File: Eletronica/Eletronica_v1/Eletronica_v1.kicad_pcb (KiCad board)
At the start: 2 copper layers, 3 parts, among them U1 QTR-1A_REFLECTANCE_SENSOR, U2 TB6612FNG

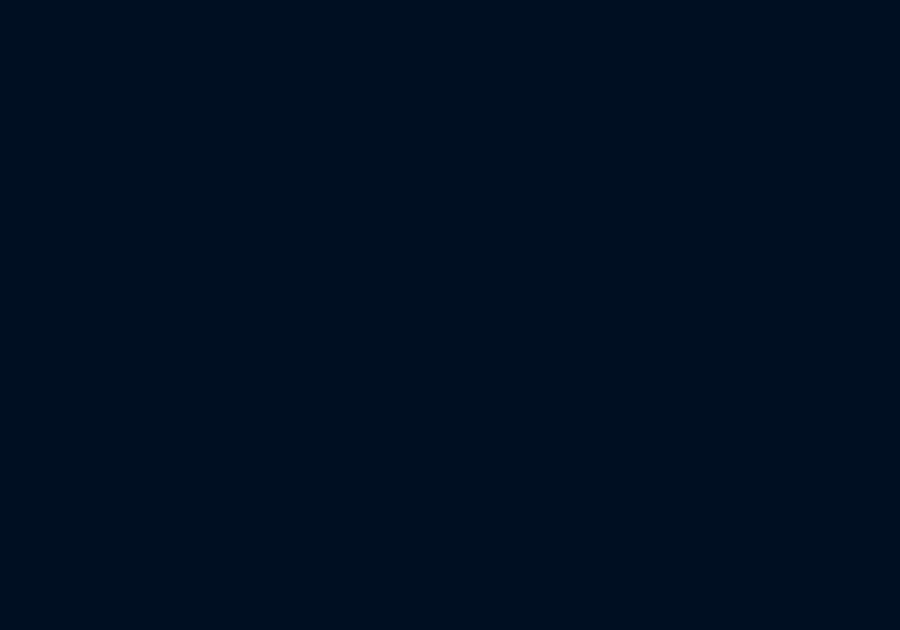
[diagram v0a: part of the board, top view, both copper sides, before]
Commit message: Corrigido circuito de alimentação e conexão dos periféricos
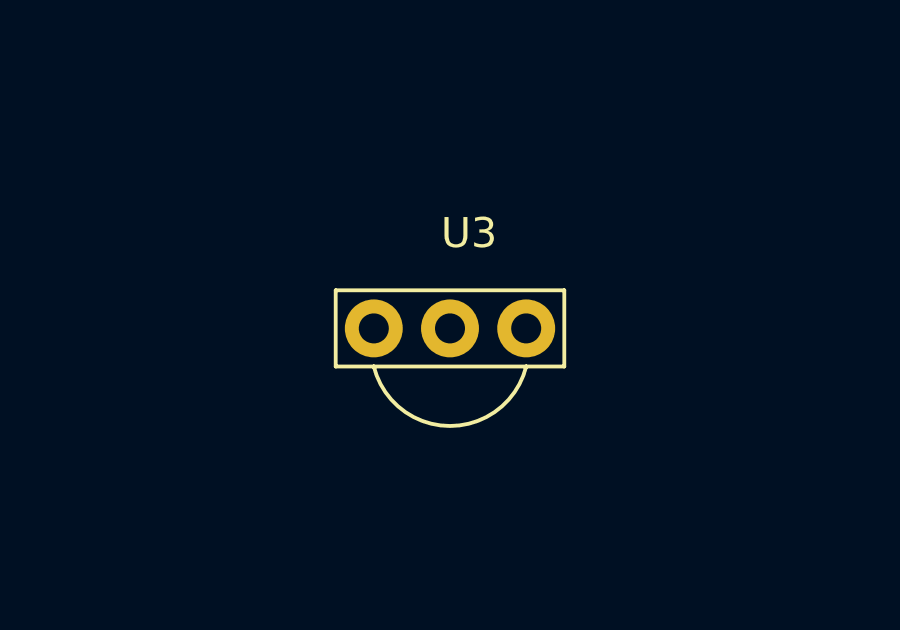
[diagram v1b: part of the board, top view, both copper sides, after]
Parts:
- added U3: TSOP1838, TSOP1838:TSOP1838, F.Cu at (118.4, 69.3)

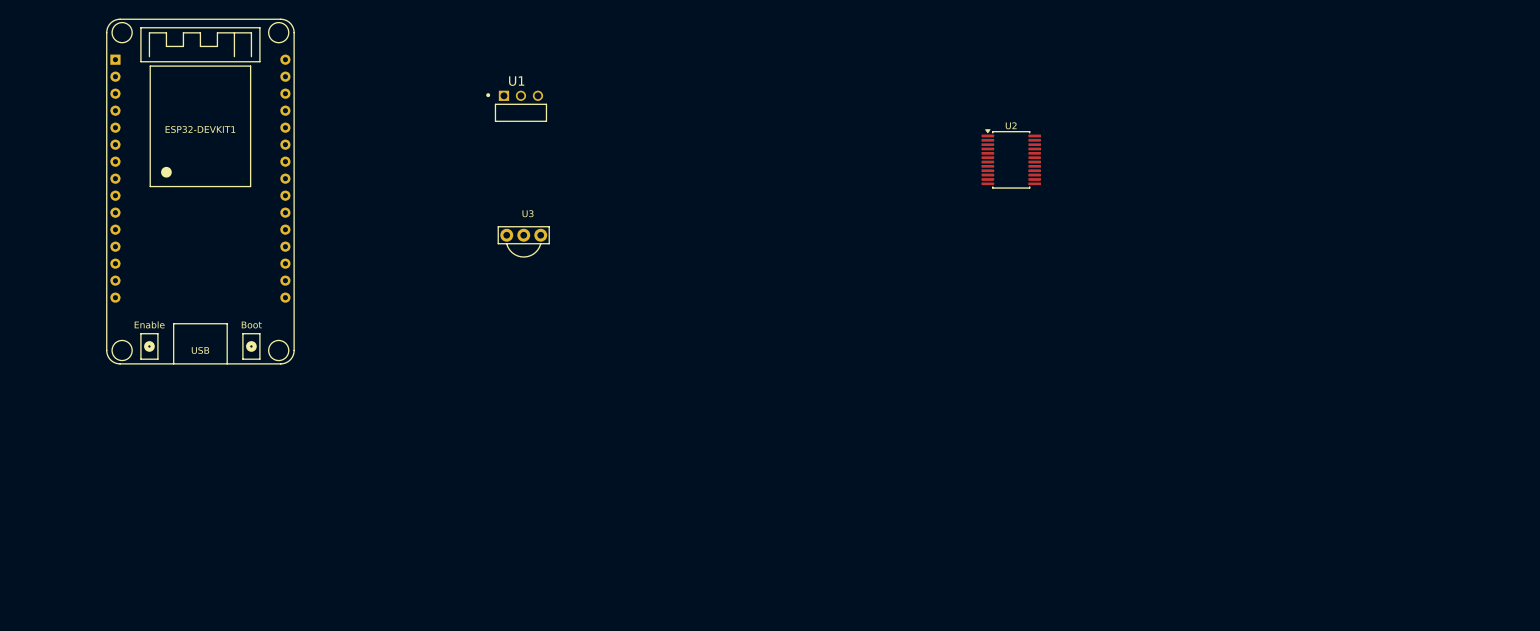
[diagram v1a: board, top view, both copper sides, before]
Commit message: Atualizado swtich e footprints
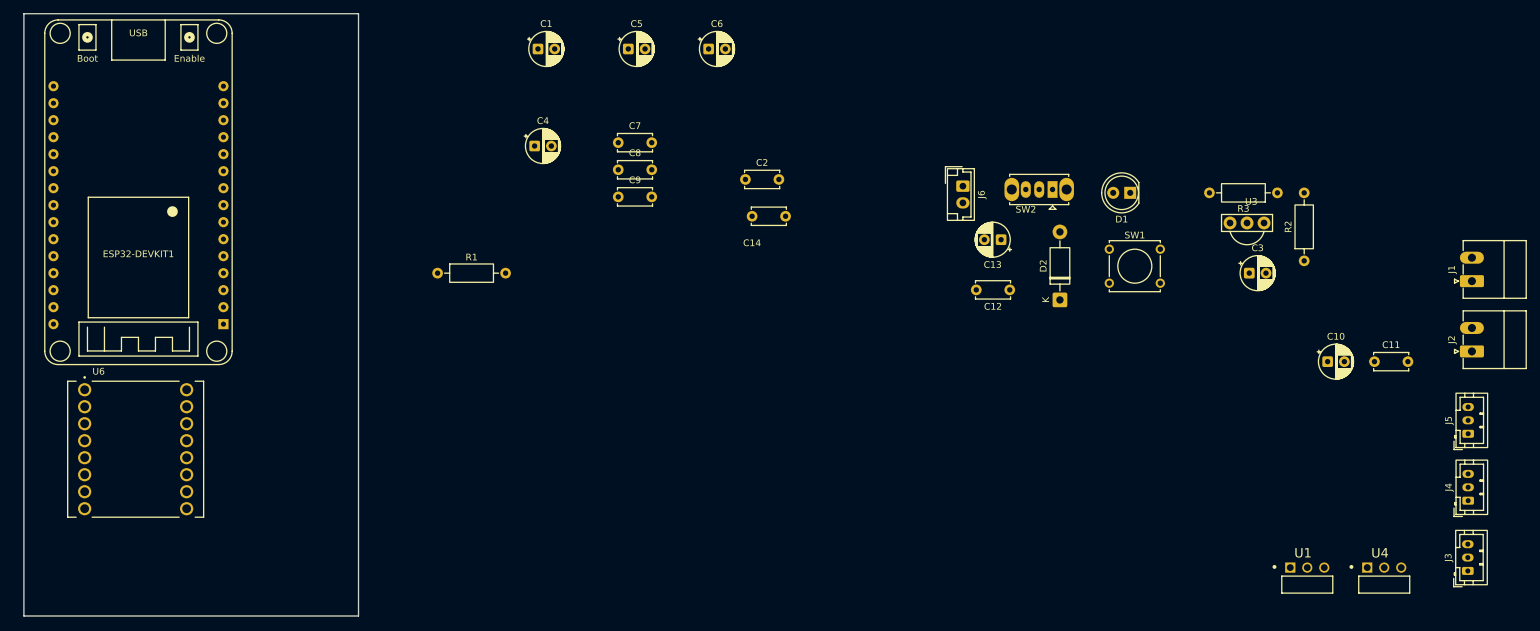
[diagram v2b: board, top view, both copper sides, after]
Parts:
- removed U2: TB6612FNG, Package_SO:SSOP-24_5.3x8.2mm_P0.65mm
- added C1: 10uF, Capacitor_THT:CP_Radial_D5.0mm_P2.50mm, F.Cu at (120.5, 41.5)
- added C10: 10uF, Capacitor_THT:CP_Radial_D5.0mm_P2.50mm, F.Cu at (238.5, 88.2)
- added C11: 100nF, Capacitor_THT:C_Disc_D5.0mm_W2.5mm_P5.00mm, F.Cu at (245.5, 88.2)
- added C12: 100nF, Capacitor_THT:C_Disc_D5.0mm_W2.5mm_P5.00mm, F.Cu at (191.0, 77.5)
- added C13: 10uF, Capacitor_THT:CP_Radial_D5.0mm_P2.50mm, F.Cu at (189.7, 70.0)
- added C14: 100nF, Capacitor_THT:C_Disc_D5.0mm_W2.5mm_P5.00mm, F.Cu at (152.5, 66.5)
- added C2: 100nF, Capacitor_THT:C_Disc_D5.0mm_W2.5mm_P5.00mm, F.Cu at (151.5, 61.0)
- added C3: 4.7uF, Capacitor_THT:CP_Radial_D5.0mm_P2.50mm, F.Cu at (226.8, 75.0)
- added C4: 10uF, Capacitor_THT:CP_Radial_D5.0mm_P2.50mm, F.Cu at (120.0, 56.0)
- added C5: 10uF, Capacitor_THT:CP_Radial_D5.0mm_P2.50mm, F.Cu at (134.0, 41.5)
- added C6: 10uF, Capacitor_THT:CP_Radial_D5.0mm_P2.50mm, F.Cu at (146.0, 41.5)
- added C7: 100nF, Capacitor_THT:C_Disc_D5.0mm_W2.5mm_P5.00mm, F.Cu at (132.5, 55.5)
- added C8: 100nF, Capacitor_THT:C_Disc_D5.0mm_W2.5mm_P5.00mm, F.Cu at (132.5, 59.5)
- added C9: 100nF, Capacitor_THT:C_Disc_D5.0mm_W2.5mm_P5.00mm, F.Cu at (132.5, 63.6)
- added D1: LED, LED_THT:LED_D5.0mm, F.Cu at (209.0, 63.0)
- added D2: 1N4007, Diode_THT:D_DO-41_SOD81_P10.16mm_Horizontal, F.Cu at (198.5, 79.0)
- added J1: Motor_R, Connector_Phoenix_MC:PhoenixContact_MC_1,5_2-G-3.5_1x02_P3.50mm_Horizontal, F.Cu at (260.1, 76.2)
- added J2: Motor_L, Connector_Phoenix_MC:PhoenixContact_MC_1,5_2-G-3.5_1x02_P3.50mm_Horizontal, F.Cu at (260.1, 86.7)
- added J3: Sharp_G2Y0A41SK, Connector_JST:JST_PH_B3B-PH-K_1x03_P2.00mm_Vertical, F.Cu at (259.4, 119.5)
- added J4: Sharp_G2Y0A41SK, Connector_JST:JST_PH_B3B-PH-K_1x03_P2.00mm_Vertical, F.Cu at (259.5, 109.0)
- added J5: Sharp_G2Y0A41SK, Connector_JST:JST_PH_B3B-PH-K_1x03_P2.00mm_Vertical, F.Cu at (259.5, 99.0)
- added J6: Bateria, Connector_JST:JST_EH_B2B-EH-A_1x02_P2.50mm_Vertical, F.Cu at (184.0, 62.0)
- added R1: 300, Resistor_THT:R_Axial_DIN0207_L6.3mm_D2.5mm_P10.16mm_Horizontal, F.Cu at (105.5, 75.0)
- added R2: 100, Resistor_THT:R_Axial_DIN0207_L6.3mm_D2.5mm_P10.16mm_Horizontal, F.Cu at (235.0, 73.2)
- added R3: 10k, Resistor_THT:R_Axial_DIN0207_L6.3mm_D2.5mm_P10.16mm_Horizontal, F.Cu at (231.0, 63.0)
- added SW1: TROCA_MODO, Button_Switch_THT:SW_Tactile_Straight_KSA0Axx1LFTR, F.Cu at (205.9, 71.4)
- added SW2: SW_SPDT, Button_Switch_THT:SW_Slide_SPDT_Straight_CK_OS102011MS2Q, F.Cu at (197.4, 62.5)
- added U4: QTR-1A_REFLECTANCE_SENSOR, QTR-1A_REFLECTANCE_SENSOR:SENSOR_QTR-1A_REFLECTANCE_SENSOR, F.Cu at (247.0, 121.5)
- added U6: ROB-14450, ROB-14450:MODULE_ROB-14450, F.Cu at (60.4, 101.3)
- moved U1 137.0 mm to (235.5, 121.5)
- moved U3 108.1 mm to (226.5, 67.5)
- moved ESP32-DEVKIT1 40.6 mm to (60.8, 82.6), turned to 180 degrees
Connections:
- ESP32-DEVKIT1 pad 13: unconnected-(ESP32-DEVKIT1-ADC2_4/13-Pad13) -> MODE_SWT
- ESP32-DEVKIT1 pad 14: unconnected-(ESP32-DEVKIT1-GND-Pad14) -> GND
- ESP32-DEVKIT1 pad 15: unconnected-(ESP32-DEVKIT1-VIN-Pad15) -> VCC 5V
- ESP32-DEVKIT1 pad 16: unconnected-(ESP32-DEVKIT1-3V3-Pad16) -> 3V3
- ESP32-DEVKIT1 pad 17: unconnected-(ESP32-DEVKIT1-GND-Pad17) -> GND
- ESP32-DEVKIT1 pad 2: unconnected-(ESP32-DEVKIT1-ADC1_0/36/VP-Pad2) -> IR_L
- ESP32-DEVKIT1 pad 24: unconnected-(ESP32-DEVKIT1-SCK/18-Pad24) -> PWM_MOTOR_R
- ESP32-DEVKIT1 pad 25: unconnected-(ESP32-DEVKIT1-MISO/19-Pad25) -> MOTOR_R_IN1
- ESP32-DEVKIT1 pad 26: unconnected-(ESP32-DEVKIT1-SDA/21-Pad26) -> MOTOR_R_IN2
- ESP32-DEVKIT1 pad 29: unconnected-(ESP32-DEVKIT1-SCL/22-Pad29) -> PWM_MOTOR_L
- ESP32-DEVKIT1 pad 30: unconnected-(ESP32-DEVKIT1-MOSI/23-Pad30) -> MOTOR_L_IN1
- ESP32-DEVKIT1 pad 4: unconnected-(ESP32-DEVKIT1-ADC1_6/34-Pad4) -> IR_F
- ESP32-DEVKIT1 pad 5: unconnected-(ESP32-DEVKIT1-ADC1_7/35-Pad5) -> IR_R
- ESP32-DEVKIT1 pad 6: unconnected-(ESP32-DEVKIT1-ADC1_4/32-Pad6) -> QTR_L
- ESP32-DEVKIT1 pad 7: unconnected-(ESP32-DEVKIT1-ADC1_5/33-Pad7) -> QTR_R
- ESP32-DEVKIT1 pad 8: unconnected-(ESP32-DEVKIT1-ADC2_8/25-Pad8) -> MOTOR_L_IN2
- ESP32-DEVKIT1 pad 9: unconnected-(ESP32-DEVKIT1-ADC2_9/26-Pad9) -> STBY
- U1 pad 1: unconnected-(U1-GND-Pad1) -> GND
- U1 pad 2: unconnected-(U1-VIN-Pad2) -> VCC 5V
- U1 pad 3: unconnected-(U1-OUT-Pad3) -> QTR_R
- U3 pad 1: unconnected-(U3-OUT-Pad1) -> INFRA_OUT
- U3 pad 2: unconnected-(U3-GND-Pad2) -> GND
- U3 pad 3: unconnected-(U3-VCC-Pad3) -> Net-(U3-VCC)
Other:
- board outline added: 50 x 90 mm

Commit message: Reduzido Capacitores, e tracado layout parcial da pcb
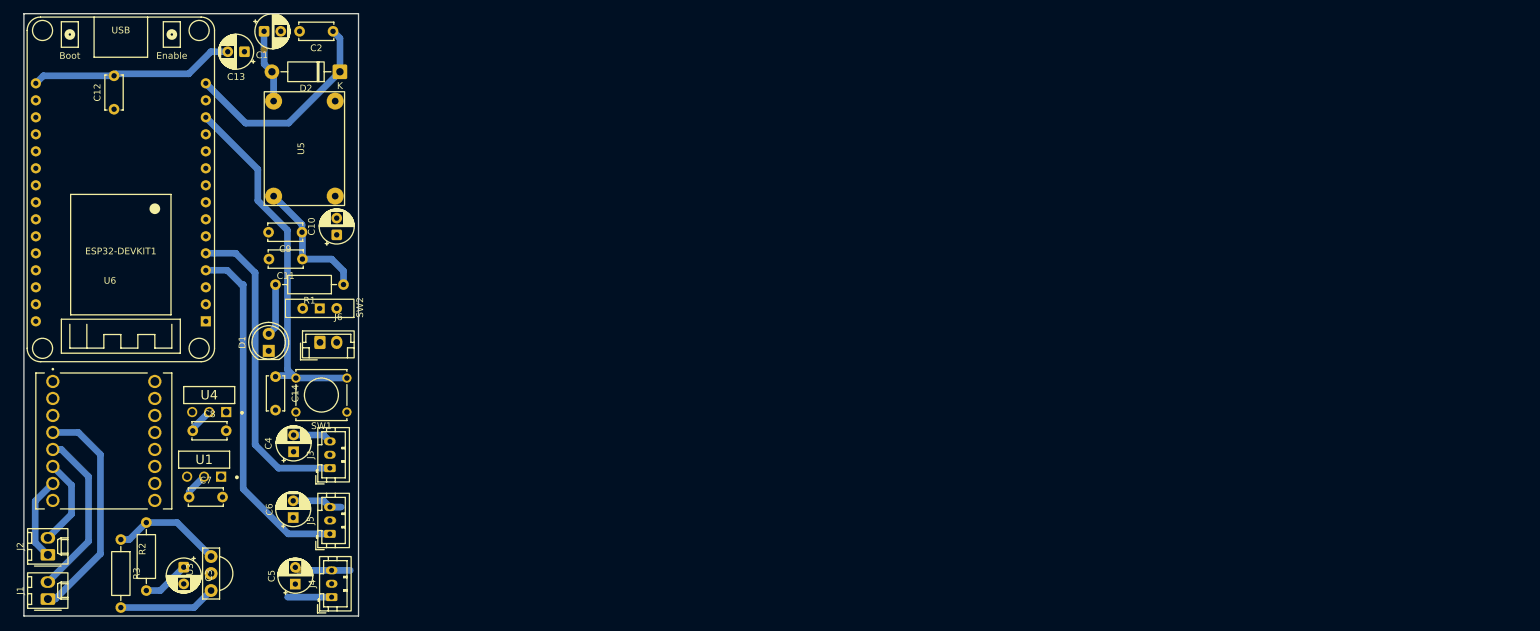
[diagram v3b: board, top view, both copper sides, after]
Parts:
- added U5: Mini560, Buck_Converter_4r7:Sem título, F.Cu at (85.6, 56.4)
- C4, C5, C6: value 10uF -> 10 uF; footprint Capacitor_THT:CP_Radial_D5.0mm_P2.50mm -> PCM_Capacitor_THT_AKL:CP_Radial_D5.0mm_P2.50mm
- J1, J2: footprint Connector_Phoenix_MC:PhoenixContact_MC_1,5_2-G-3.5_1x02_P3.50mm_Horizontal -> Connector_Molex:Molex_KK-254_AE-6410-02A_1x02_P2.54mm_Vertical
- SW2: footprint Button_Switch_THT:SW_Slide_SPDT_Straight_CK_OS102011MS2Q -> Button_Switch_THT:SW_Slide-03_Wuerth-WS-SLTV_10x2.5x6.4_P2.54mm
- moved J1 218.0 mm to (47.3, 123.7)
- moved J2 215.0 mm to (47.3, 117.1)
- moved R3 180.4 mm to (58.2, 114.8), turned to -90 degrees
- moved R2 179.9 mm to (62.0, 122.4)
- moved U4 177.9 mm to (71.4, 93.2), turned to 180 degrees
- moved J5 170.7 mm to (89.4, 114.0)
- moved J3 170.7 mm to (89.4, 104.1)
- moved J4 170.4 mm to (89.7, 123.4)
- moved U1 165.9 mm to (70.6, 102.9), turned to 180 degrees
- moved C3 165.2 mm to (67.6, 118.9), turned to -90 degrees
- moved U3 163.4 mm to (71.7, 119.9), turned to 90 degrees
- moved C11 160.9 mm to (85.3, 72.9), turned to 180 degrees
- moved C10 149.3 mm to (90.4, 69.3), turned to 90 degrees
- moved C12 136.5 mm to (57.1, 50.5), turned to 90 degrees
- moved D1 130.9 mm to (80.3, 86.6), turned to 90 degrees
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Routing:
- net VCC 5V: track 0.00 -> 61.1 mm
- net MODE_SWT: track 0.00 -> 55.5 mm
- net IR_F: track 0.00 -> 52.7 mm
- net IR_R: track 0.00 -> 46.9 mm
- net 3V3: track 0.00 -> 37.3 mm
- net Net-(J1-Pin_1): track 0.00 -> 34.0 mm
- net Net-(J1-Pin_2): track 0.00 -> 25.3 mm
- net BAT: track 0.00 -> 20.1 mm
- net Net-(U3-VCC): track 0.00 -> 16.6 mm
- net INFRA_OUT: track 0.00 -> 14.5 mm
- net Net-(J2-Pin_2): track 0.00 -> 13.3 mm
- net Net-(J2-Pin_1): track 0.00 -> 12.6 mm
- net Net-(D2-A): track 0.00 -> 11.0 mm
- net Net-(D1-A): track 0.00 -> 7.79 mm
- net IR_L: track 0.00 -> 6.59 mm
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
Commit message: Finalizado a versao funcional da placa
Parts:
- removed C10: 10uF, Capacitor_THT:CP_Radial_D5.0mm_P2.50mm
- removed C11: 100nF, Capacitor_THT:C_Disc_D5.0mm_W2.5mm_P5.00mm
- moved R3 73.2 mm to (84.4, 46.4)
- moved U3 69.8 mm to (87.8, 52.0)
- moved R2 66.7 mm to (69.9, 56.2), turned to 0 degrees
- moved C3 57.1 mm to (62.7, 62.0), turned to 180 degrees
- moved J6 56.7 mm to (47.2, 45.9), turned to 90 degrees
- moved SW1 54.5 mm to (70.0, 45.9), turned to 90 degrees
- moved SW2 50.1 mm to (53.4, 43.9), turned to -90 degrees
- moved D1 48.2 mm to (63.1, 41.6)
- moved J1 45.7 mm to (52.0, 78.2), turned to -90 degrees
- moved R1 44.3 mm to (57.5, 48.3), turned to 90 degrees
- moved C14 42.3 mm to (75.1, 48.6), turned to 180 degrees
- moved U5 36.3 mm to (50.5, 65.8)
- moved C1 35.9 mm to (46.3, 52.3)
- moved C9 34.4 mm to (60.3, 45.2), turned to 0 degrees
- moved C13 33.1 mm to (60.2, 70.6), turned to 0 degrees
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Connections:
- ESP32-DEVKIT1 pad 11: unconnected-(ESP32-DEVKIT1-ADC2_6/14-Pad11) -> MODE_SWT
- ESP32-DEVKIT1 pad 13: MODE_SWT -> INFRA_OUT
- ESP32-DEVKIT1 pad 22: unconnected-(ESP32-DEVKIT1-TXD_2/17-Pad22) -> PWM_MOTOR_R
- ESP32-DEVKIT1 pad 23: unconnected-(ESP32-DEVKIT1-SS/5-Pad23) -> MOTOR_R_IN2
- ESP32-DEVKIT1 pad 24: PWM_MOTOR_R -> MOTOR_R_IN1
- ESP32-DEVKIT1 pad 25: MOTOR_R_IN1 -> STBY
- ESP32-DEVKIT1 pad 26: MOTOR_R_IN2 -> MOTOR_L_IN1
- ESP32-DEVKIT1 pad 27: unconnected-(ESP32-DEVKIT1-RXD_0/3-Pad27) -> MOTOR_L_IN2
- ESP32-DEVKIT1 pad 28: unconnected-(ESP32-DEVKIT1-TXD_0/1-Pad28) -> PWM_MOTOR_L
- ESP32-DEVKIT1 pad 29: PWM_MOTOR_L -> unconnected-(ESP32-DEVKIT1-SCL/22-Pad29)
- ESP32-DEVKIT1 pad 30: MOTOR_L_IN1 -> unconnected-(ESP32-DEVKIT1-MOSI/23-Pad30)
- ESP32-DEVKIT1 pad 8: MOTOR_L_IN2 -> unconnected-(ESP32-DEVKIT1-ADC2_8/25-Pad8)
- ESP32-DEVKIT1 pad 9: STBY -> unconnected-(ESP32-DEVKIT1-ADC2_9/26-Pad9)
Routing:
- net VCC 5V: track 61.1 -> 202.5 mm
- net GND: track 1.28 -> 67.4 mm, vias 0 -> 14
- net QTR_R: track 0.00 -> 54.6 mm
- net QTR_L: track 0.00 -> 44.5 mm
- net BAT: track 20.1 -> 50.7 mm
- net IR_F: track 52.7 -> 24.8 mm
- net 3V3: track 37.3 -> 57.9 mm
- net Net-(J1-Pin_1): track 34.0 -> 16.6 mm
- net MODE_SWT: track 55.5 -> 42.4 mm
- net INFRA_OUT: track 14.5 -> 26.6 mm
- net IR_R: track 46.9 -> 36.4 mm
- net IR_L: track 6.59 -> 16.9 mm
- net Net-(J1-Pin_2): track 25.3 -> 15.9 mm
- net Net-(J6-Pin_2): track 0.00 -> 7.13 mm
- net Net-(D2-A): track 11.0 -> 16.4 mm
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- added copper zone on B.Cu, net GND
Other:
- outline, holes or cut-outs redrawn
